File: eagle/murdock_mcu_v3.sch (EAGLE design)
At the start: 31 parts, among them IC1 MPU-9150, IC2 LT1763CS8-3.3, IC3 STM32F4XX_64, IC4 BMP085, Q2 PFET, U1 USD-SOCKETNEW, X1 USBSMD, X2 MURDOCK_STACK

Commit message: usb placement & smaller tantal
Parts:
- C1, C2: device rcl:CPOL-EUSMCD -> rcl:CPOL-EUSMCC
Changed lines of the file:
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@@
 <part name="P+1" library="supply1" deviceset="+5V" device=""/>
 <part name="+3V1" library="supply1" deviceset="+3V3" device=""/>
-<part name="C1" library="rcl" deviceset="CPOL-EU" device="SMCD" value="47µF/10V"/>
-<part name="C2" library="rcl" deviceset="CPOL-EU" device="SMCD" value="100µF/6V"/>
+<part name="C1" library="rcl" deviceset="CPOL-EU" device="SMCC" value="47µF/10V"/>
+<part name="C2" library="rcl" deviceset="CPOL-EU" device="SMCC" value="100µF/6V"/>
 <part name="+3V2" library="supply1" deviceset="+3V3" device=""/>
 <part name="+3V3" library="supply1" deviceset="+3V3" device=""/>

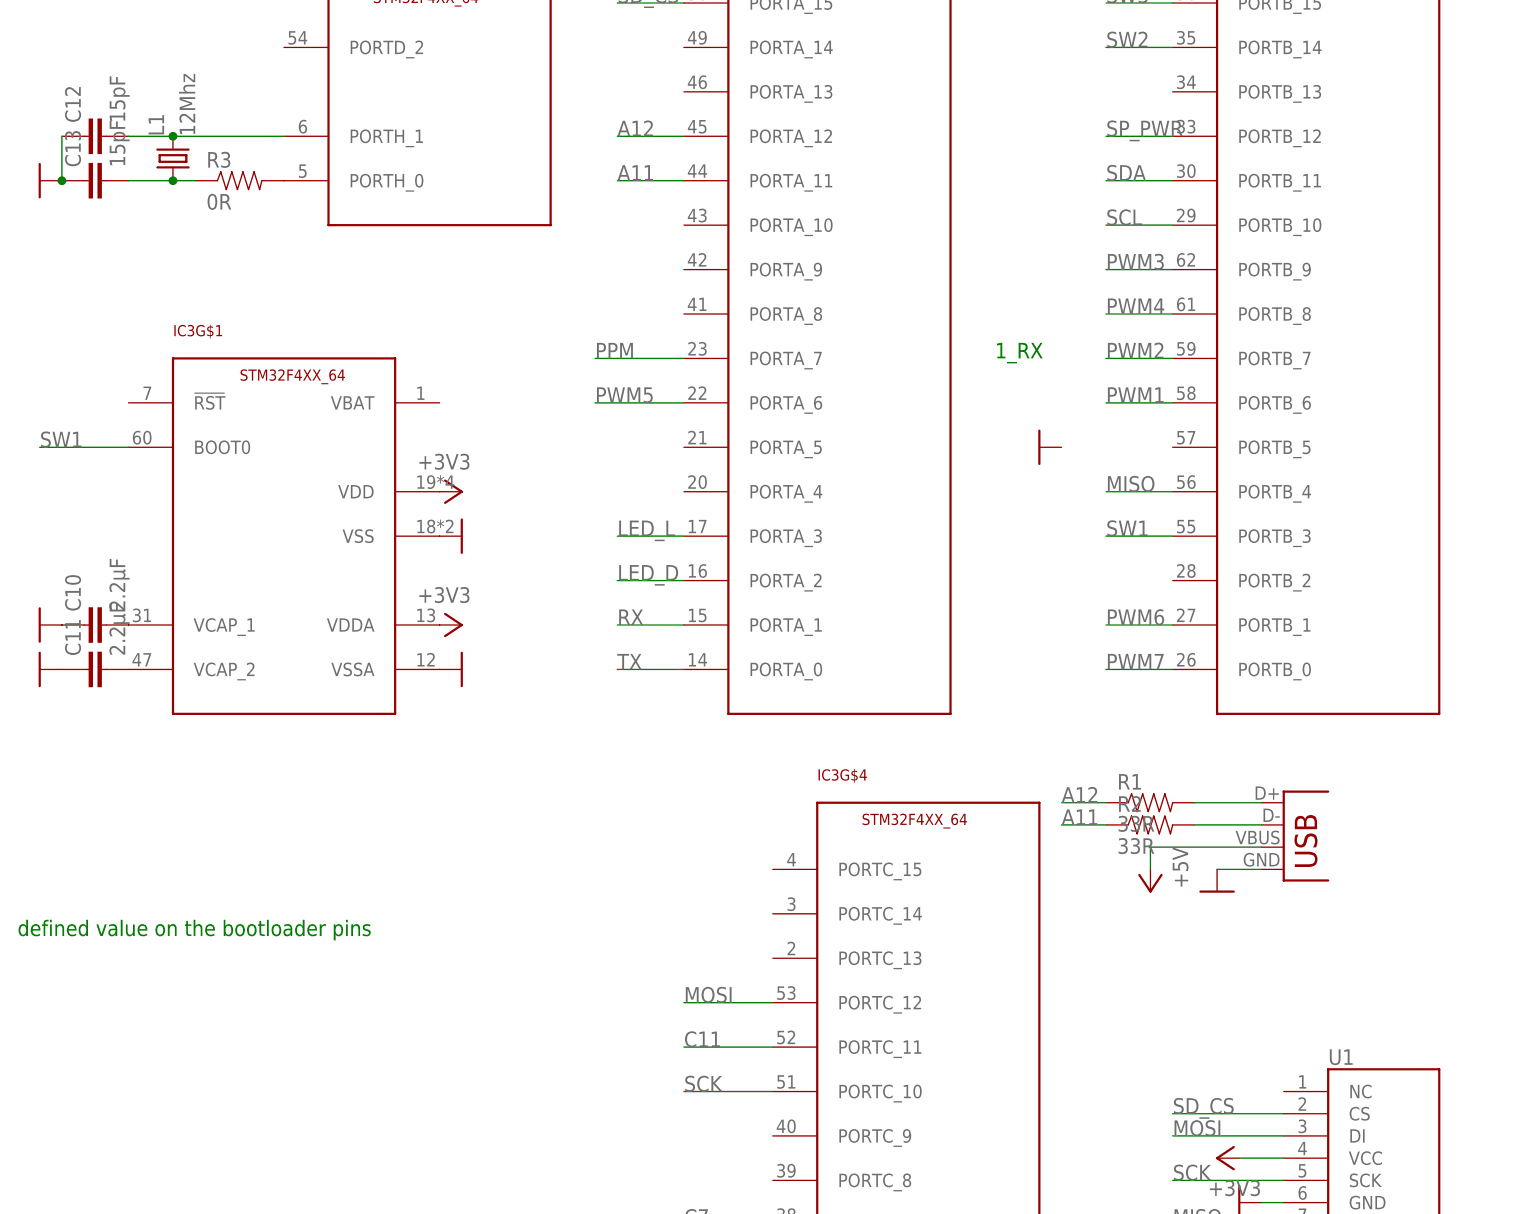
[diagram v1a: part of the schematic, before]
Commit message: bootloader robustness
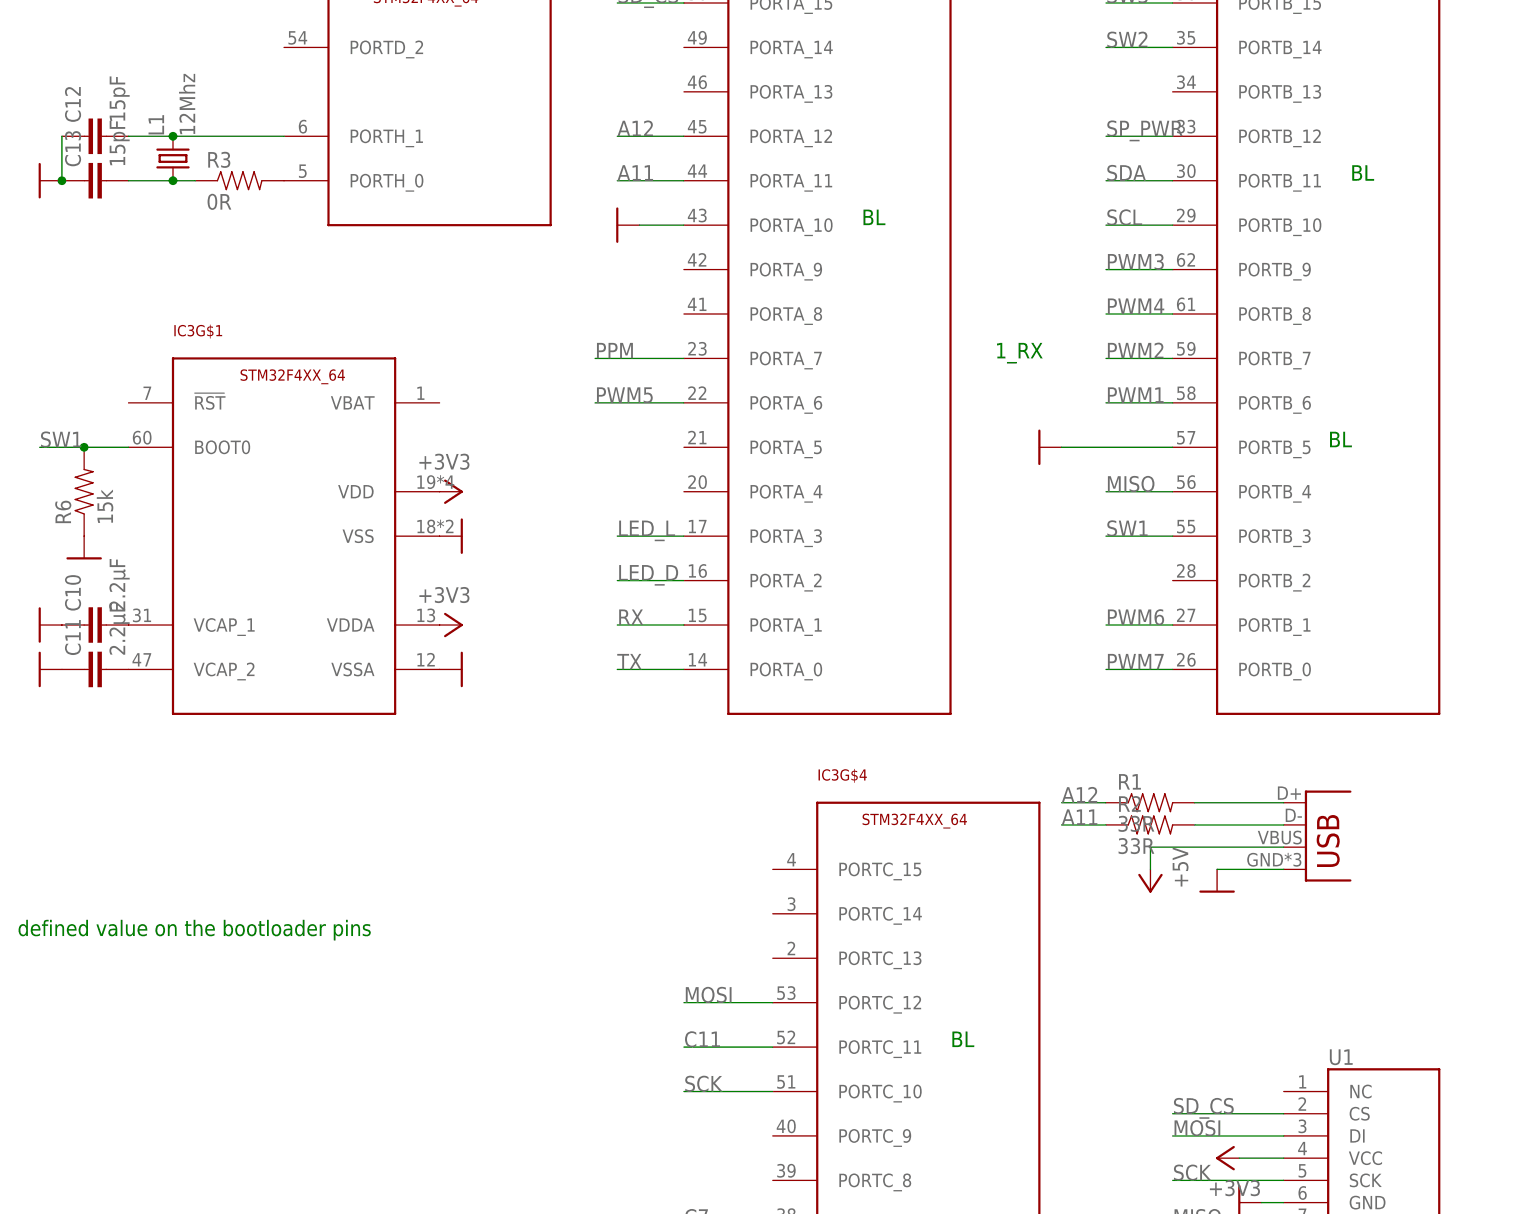
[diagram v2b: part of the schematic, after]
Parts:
- removed X1: USBSMD, SparkFun-Connectors:USBSMD
- added JP1: USB-MICROB, SparkFun-Connectors:USB-MICROB
- added R6: 15k, SparkFun:RESISTOR0402-RES
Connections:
- net +5V: now also JP1.VBUS; no longer X1.VBUS
- net GND: now also IC3G$2.PORTA_10, IC3G$3.PORTB_5, JP1.GND, R6.1; no longer X1.GND
- net N$1: now also JP1.D-; no longer X1.D-
- net N$2: now also JP1.D+; no longer X1.D+
- net SW1: now also R6.2
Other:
- note added: "BL"
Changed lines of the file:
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@@
 <parts>
 <part name="IC3" library="stm32" deviceset="STM32F4XX_64" device=""/>
-<part name="X1" library="SparkFun-Connectors" deviceset="USB" device="SMD"/>
 <part name="U1" library="SparkFun-Connectors" deviceset="USD-SOCKET" device="NEW"/>
 <part name="X2" library="murdock" deviceset="MURDOCK_STACK" device=""/>
@@
 <part name="+3V12" library="supply1" deviceset="+3V3" device=""/>
 <part name="GND8" library="supply1" deviceset="GND" device=""/>
+<part name="JP1" library="SparkFun-Connectors" deviceset="USB" device="-MICROB"/>
+<part name="GND9" library="SparkFun-Aesthetics" deviceset="GND" device=""/>
+<part name="R6" library="SparkFun" deviceset="RESISTOR" device="0402-RES" value="15k"/>
+<part name="GND16" library="SparkFun-Aesthetics" deviceset="GND" device=""/>
 </parts>
 <sheets>
@@
 <text x="17.78" y="127" size="1.778" layer="91">1_RX</text>
 <text x="93.98" y="-10.16" size="1.778" layer="91">in case of 5V, pull up is neccessary (and proper pin configuraiotn)</text>
+<text x="2.54" y="142.24" size="1.778" layer="91">BL</text>
+<text x="58.42" y="147.32" size="1.778" layer="91">BL</text>
+<text x="12.7" y="48.26" size="1.778" layer="91">BL</text>
+<text x="55.88" y="116.84" size="1.778" layer="91">BL</text>
 </plain>
 <instances>
@@
 <instance part="IC3" gate="G$4" x="-2.54" y="-12.7"/>
 <instance part="IC3" gate="G$5" x="-58.42" y="142.24"/>
-<instance part="X1" gate="G$1" x="50.8" y="68.58"/>
 <instance part="U1" gate="G$1" x="58.42" y="30.48"/>
 <instance part="X2" gate="G$1" x="119.38" y="38.1"/>
@@
 <instance part="+3V12" gate="G$1" x="335.28" y="160.02" rot="R270"/>
 <instance part="GND8" gate="1" x="335.28" y="167.64" rot="R90"/>
+<instance part="JP1" gate="G$1" x="53.34" y="68.58"/>
+<instance part="GND9" gate="1" x="-25.4" y="142.24" smashed="yes" rot="R270"/>
+<instance part="R6" gate="G$1" x="-86.36" y="111.76" rot="R90"/>
+<instance part="GND16" gate="1" x="-86.36" y="104.14" smashed="yes"/>
 </instances>
 <busses>
@@
 </segment>
 <segment>
-<pinref part="X1" gate="G$1" pin="GND"/>
 <pinref part="GND2" gate="1" pin="GND"/>
-<wire x1="48.26" y1="68.58" x2="43.18" y2="68.58" width="0.1524" layer="91"/>
+<wire x1="50.8" y1="68.58" x2="43.18" y2="68.58" width="0.1524" layer="91"/>
+<pinref part="JP1" gate="G$1" pin="GND"/>
 </segment>
 <segment>
@@
 <pinref part="GND8" gate="1" pin="GND"/>
 </segment>
+<segment>
+<pinref part="IC3" gate="G$2" pin="PORTA_10"/>
+<pinref part="GND9" gate="1" pin="GND"/>
+<wire x1="-22.86" y1="142.24" x2="-17.78" y2="142.24" width="0.1524" layer="91"/>
+</segment>
+<segment>
+<pinref part="IC3" gate="G$3" pin="PORTB_5"/>
+<pinref part="GND15" gate="1" pin="GND"/>
+<wire x1="25.4" y1="116.84" x2="38.1" y2="116.84" width="0.1524" layer="91"/>
+</segment>
+<segment>
+<pinref part="R6" gate="G$1" pin="1"/>
+<pinref part="GND16" gate="1" pin="GND"/>
+</segment>
 </net>
 <net name="+3V3" class="0">
@@
 <pinref part="P+2" gate="1" pin="+5V"/>
 <wire x1="35.56" y1="68.58" x2="35.56" y2="71.12" width="0.1524" layer="91"/>
-<pinref part="X1" gate="G$1" pin="VBUS"/>
-<wire x1="35.56" y1="71.12" x2="48.26" y2="71.12" width="0.1524" layer="91"/>
+<wire x1="35.56" y1="71.12" x2="50.8" y2="71.12" width="0.1524" layer="91"/>
+<pinref part="JP1" gate="G$1" pin="VBUS"/>
 </segment>
 </net>
@@
 <net name="N$1" class="0">
 <segment>
-<pinref part="X1" gate="G$1" pin="D-"/>
-<wire x1="40.64" y1="73.66" x2="48.26" y2="73.66" width="0.1524" layer="91"/>
+<wire x1="40.64" y1="73.66" x2="50.8" y2="73.66" width="0.1524" layer="91"/>
 <pinref part="R2" gate="G$1" pin="2"/>
+<pinref part="JP1" gate="G$1" pin="D-"/>
 </segment>
 </net>
 <net name="N$2" class="0">
 <segment>
-<pinref part="X1" gate="G$1" pin="D+"/>
-<wire x1="48.26" y1="76.2" x2="40.64" y2="76.2" width="0.1524" layer="91"/>
+<wire x1="50.8" y1="76.2" x2="40.64" y2="76.2" width="0.1524" layer="91"/>
 <pinref part="R1" gate="G$1" pin="2"/>
+<pinref part="JP1" gate="G$1" pin="D+"/>
 </segment>
 </net>
@@
 <segment>
 <pinref part="IC3" gate="G$1" pin="BOOT0"/>
-<wire x1="-81.28" y1="116.84" x2="-91.44" y2="116.84" width="0.1524" layer="91"/>
+<wire x1="-81.28" y1="116.84" x2="-86.36" y2="116.84" width="0.1524" layer="91"/>
 <label x="-91.44" y="116.84" size="1.778" layer="95"/>
-</segment>
-<segment>
+<pinref part="R6" gate="G$1" pin="2"/>
+<wire x1="-86.36" y1="116.84" x2="-91.44" y2="116.84" width="0.1524" layer="91"/>
+<junction x="-86.36" y="116.84"/>
+</segment>
+<segment>
